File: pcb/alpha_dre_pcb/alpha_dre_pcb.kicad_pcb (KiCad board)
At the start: 2 copper layers, 243.7 x 82.5 mm, 110 parts, among them J1 AVR-ISP-6, SW1 SW_Push, U1 ATmega32U4-AU, U2 PRTR5V0U2X, Y1 16MHz

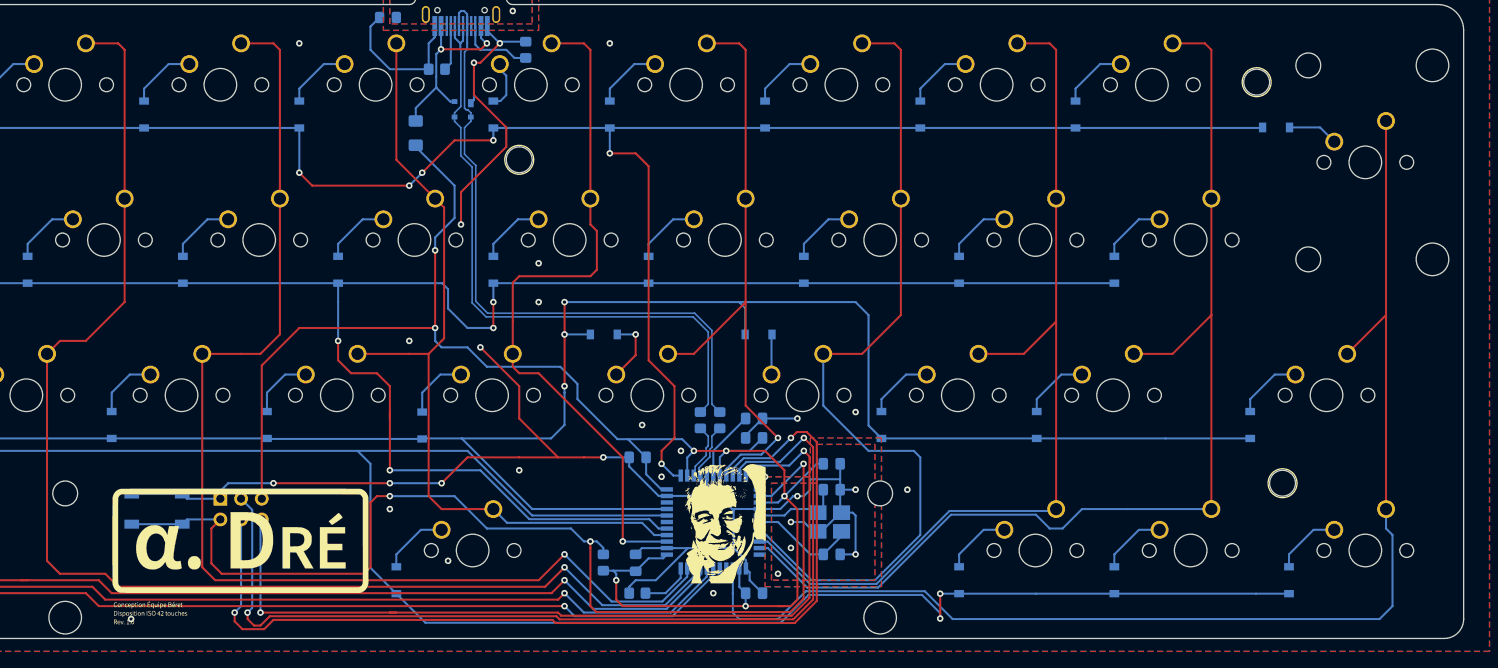
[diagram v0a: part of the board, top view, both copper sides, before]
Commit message: Rework one the case
Rev 2 case with tighter space between caps and case

Start the conception of 3D printed case (integrated)
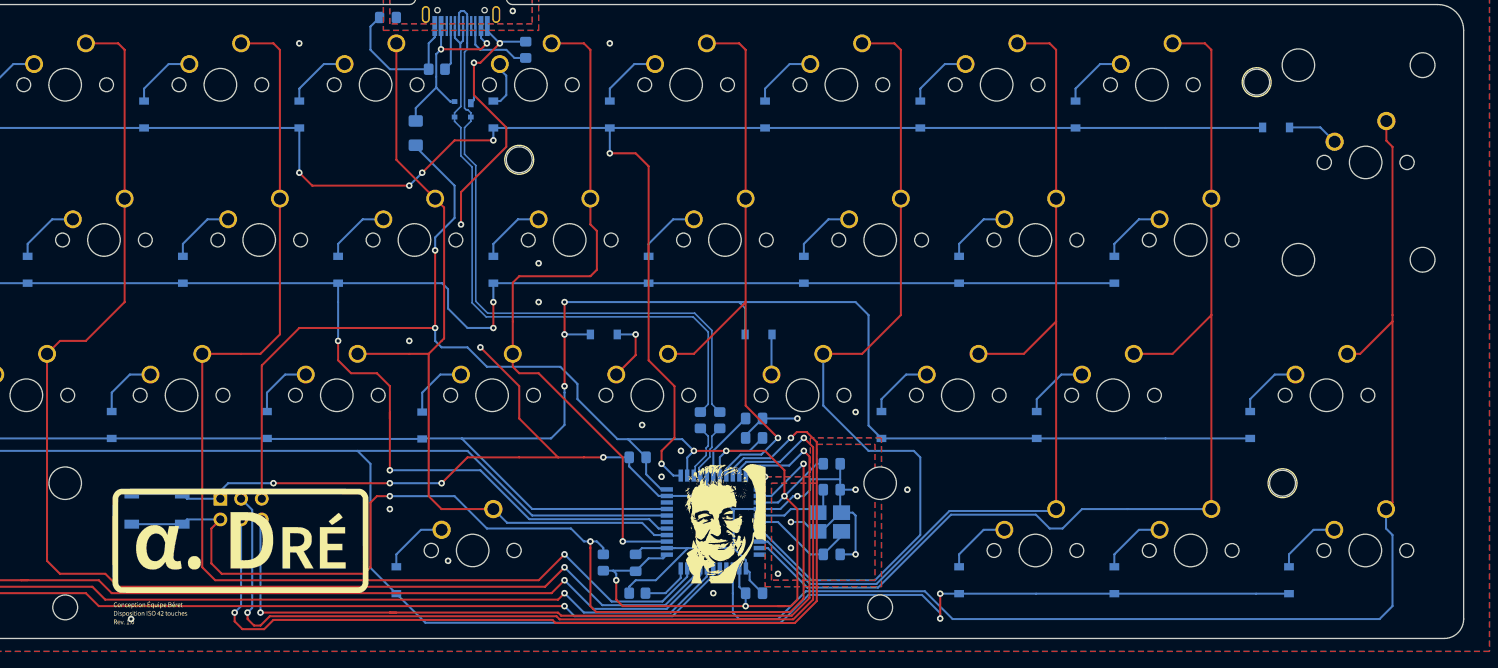
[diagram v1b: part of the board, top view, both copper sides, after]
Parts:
- MX1, MX10, MX11, MX12, MX13, MX14, MX15, MX16, MX17, MX18, MX19, MX20, MX21, MX23, MX24, MX25, MX26, MX27, MX28, MX29, MX3, MX30, MX31, MX32, MX33, MX34, MX35, MX36, MX37, MX38, MX39, MX5, MX6, MX7, MX8, MX9: footprint isio42_pcb:SW_Cherry_MX_1.00u_PCB_perso -> alpha_dre_footprints:SW_Cherry_MX_1.00u_PCB_perso
- MX2: footprint isio42_pcb:SW_Cherry_MX_1.50u_PCB_perso -> alpha_dre_footprints:SW_Cherry_MX_1.50u_PCB_perso
- MX22: footprint isio42_pcb:SW_Cherry_MX_6.25u_PCB_perso -> MX_Only:MXOnly-6.25U-ReversedStabilizers-NoLED
- MX4, MX42: footprint isio42_pcb:SW_Cherry_MX_1.25u_PCB_perso -> alpha_dre_footprints:SW_Cherry_MX_1.25u_PCB_perso
- MX40: footprint isio42_pcb:SW_Cherry_MX_ISOEnter_PCB_perso -> MX_Only:MXOnly-ISO-ReversedStabilizers-NoLED
- MX41: footprint isio42_pcb:SW_Cherry_MX_1.75u_PCB_perso -> alpha_dre_footprints:SW_Cherry_MX_1.75u_PCB_perso
- moved MX22 5.68 mm to (145.1, 98.7)
- moved MX40 5.67 mm to (254.7, 51.1)
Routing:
- net COL11: track 156.9 -> 158.0 mm
- net GND: vias 31 -> 28
- net (no net): vias 0 -> 2

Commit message: Add 3D printed case version and clean folders for concerning the case
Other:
- board size 243.7 x 82.5 mm -> 243.7 x 81.8 mm
